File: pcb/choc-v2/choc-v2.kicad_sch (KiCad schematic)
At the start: 139 parts, among them J1 OLED, J2 Conn_01x02_Female, J3 Conn_01x03_Female, SW1 SW_Push, SW2 RotaryEncoder_Switch, SW3 RotaryEncoder_Switch, SW4 SW_SPDT, U1 Elite-C

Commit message: Checkpoint commit.
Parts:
- removed D61, D62, D63, D64, D65: SK6812MINI, footprints:YS-SK6812MINI-E, symbol LED:SK6812MINI
- added D61, D62, D63, D64, D65: SK6812MINI, footprints:YS-SK6812MINI-E, symbol atreyu-pcb2:SK6812MINI_LED
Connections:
- net GND: now also D61.3 (VSS), D62.3 (VSS), D63.3 (VSS), D64.3 (VSS), D65.3 (VSS)
- net LED: now also D61.4 (DIN)
- net VCC: now also D61.1 (VDD), D62.1 (VDD), D63.1 (VDD), D64.1 (VDD), D65.1 (VDD)
- new net: D62.2 (DOUT), D63.4 (DIN)
- new net: D61.2 (DOUT), D62.4 (DIN)
- new net: D64.2 (DOUT), D65.4 (DIN)
- new net: D63.2 (DOUT), D64.4 (DIN)

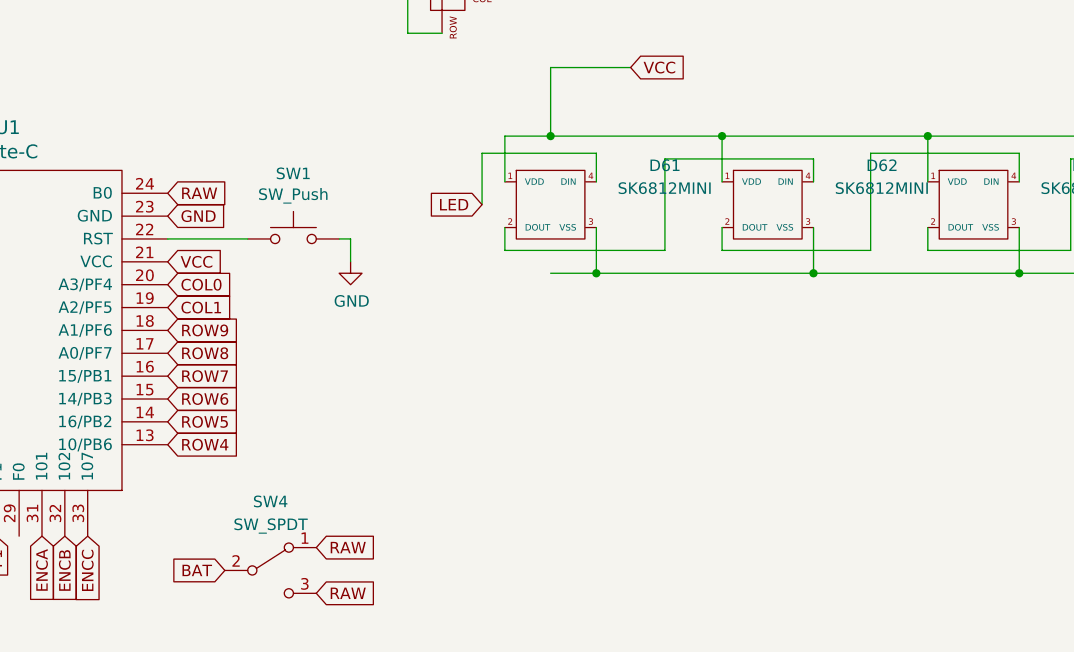
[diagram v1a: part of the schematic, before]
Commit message: Rewired choc v2 pcb.
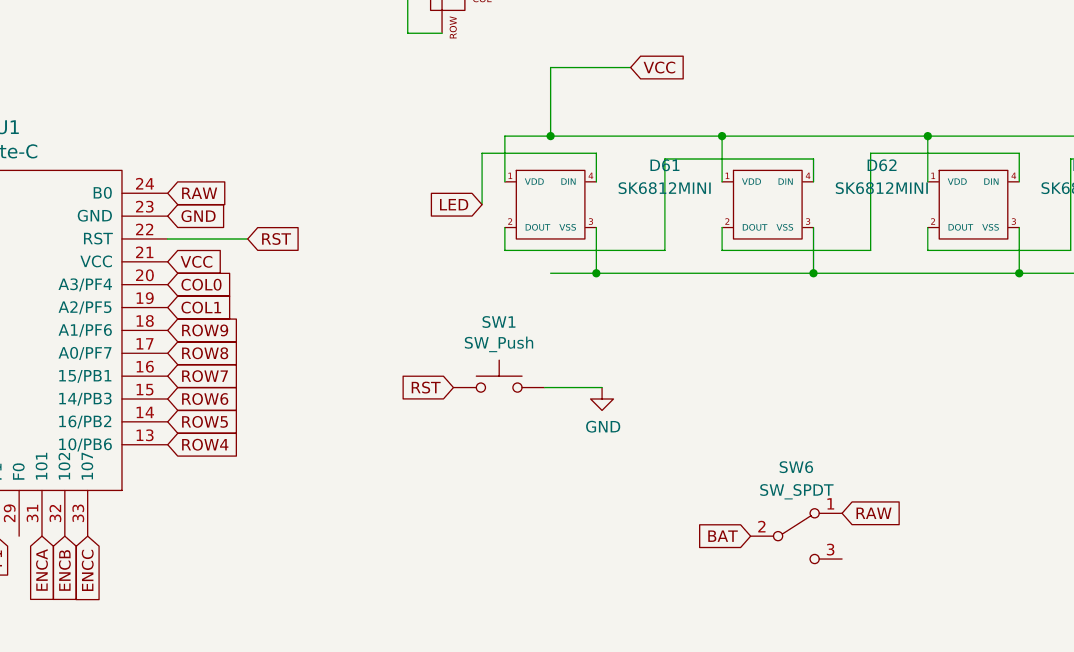
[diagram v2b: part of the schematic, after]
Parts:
- removed SW4: SW_SPDT, footprints:Switch_MSK-12C01-07, symbol Switch:SW_SPDT
- added SW6: SW_SPDT, footprints:Switch_MSK-12C01-07, symbol Switch:SW_SPDT
- SW1: footprint footprints:SW_Tactile_SPST_Angled_MJTP1117_fixed -> footprints:PushSwitch
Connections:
- net BAT: now also SW6.2 (B)
- net RAW: now also SW6.1 (A)
- net RST: now reaches SW1.1, U1.22 (RST)
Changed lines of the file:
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@@
     (stroke (width 0) (type default) (color 0 0 0 0))
   )
-  (wire (pts (xy 82.55 149.86) (xy 83.82 149.86))
-    (stroke (width 0) (type default) (color 0 0 0 0))
-  )
   (wire (pts (xy 91.44 57.15) (xy 93.98 57.15))
     (stroke (width 0) (type default) (color 0 0 0 0))
@@
     (stroke (width 0) (type default) (color 0 0 0 0))
   )
-  (wire (pts (xy 83.82 149.86) (xy 83.82 152.4))
-    (stroke (width 0) (type default) (color 0 0 0 0))
-  )
   (wire (pts (xy 99.06 35.56) (xy 99.06 52.07))
     (stroke (width 0) (type default) (color 0 0 0 0))
@@
     (stroke (width 0) (type default) (color 0 0 0 0))
   )
+  (wire (pts (xy 105.41 166.37) (xy 111.76 166.37))
+    (stroke (width 0) (type default) (color 0 0 0 0))
+  )
   (wire (pts (xy 147.955 138.43) (xy 147.955 143.51))
     (stroke (width 0) (type default) (color 0 0 0 0))
@@
     (stroke (width 0) (type default) (color 0 0 0 0))
   )
+  (global_label "RAW" (shape input) (at 138.43 180.34 0) (fields_autoplaced)
+    (effects (font (size 1.27 1.27)) (justify left))
+    (property "Intersheet References" "${INTERSHEET_REFS}" (id 0) (at 144.6531 180.4194 0)
+      (effects (font (size 1.27 1.27)) (justify left) hide)
+    )
+  )
   (global_label "GND" (shape input) (at 255.27 120.65 180) (fields_autoplaced)
     (effects (font (size 1.27 1.27)) (justify right))
@@
     )
   )
-  (global_label "RAW" (shape input) (at 80.01 189.23 0) (fields_autoplaced)
-    (effects (font (size 1.27 1.27)) (justify left))
-    (property "Intersheet References" "${INTERSHEET_REFS}" (id 0) (at 86.2331 189.3094 0)
-      (effects (font (size 1.27 1.27)) (justify left) hide)
+  (global_label "RST" (shape input) (at 95.25 166.37 180) (fields_autoplaced)
+    (effects (font (size 1.27 1.27)) (justify right))
+    (property "Intersheet References" "${INTERSHEET_REFS}" (id 0) (at 89.3898 166.4494 0)
+      (effects (font (size 1.27 1.27)) (justify right) hide)
     )
   )
@@
     )
   )
-  (global_label "BAT" (shape input) (at 69.85 186.69 180) (fields_autoplaced)
-    (effects (font (size 1.27 1.27)) (justify right))
-    (property "Intersheet References" "${INTERSHEET_REFS}" (id 0) (at 64.1107 186.7694 0)
-      (effects (font (size 1.27 1.27)) (justify right) hide)
-    )
-  )
   (global_label "ROW1" (shape input) (at 31.75 62.23 180) (fields_autoplaced)
     (effects (font (size 1.27 1.27)) (justify right))
@@
     )
   )
-  (global_label "RAW" (shape input) (at 80.01 184.15 0) (fields_autoplaced)
-    (effects (font (size 1.27 1.27)) (justify left))
-    (property "Intersheet References" "${INTERSHEET_REFS}" (id 0) (at 86.2331 184.2294 0)
-      (effects (font (size 1.27 1.27)) (justify left) hide)
-    )
-  )
   (global_label "RAW" (shape input) (at 63.5 144.78 0) (fields_autoplaced)
     (effects (font (size 1.27 1.27)) (justify left))
@@
     )
   )
+  (global_label "BAT" (shape input) (at 128.27 182.88 180) (fields_autoplaced)
+    (effects (font (size 1.27 1.27)) (justify right))
+    (property "Intersheet References" "${INTERSHEET_REFS}" (id 0) (at 122.5307 182.9594 0)
+      (effects (font (size 1.27 1.27)) (justify right) hide)
+    )
+  )
   (global_label "ROW7" (shape input) (at 179.07 77.47 180) (fields_autoplaced)
     (effects (font (size 1.27 1.27)) (justify right))
@@
     )
   )
+  (global_label "RST" (shape input) (at 72.39 149.86 0) (fields_autoplaced)
+    (effects (font (size 1.27 1.27)) (justify left))
+    (property "Intersheet References" "${INTERSHEET_REFS}" (id 0) (at 78.2502 149.7806 0)
+      (effects (font (size 1.27 1.27)) (justify left) hide)
+    )
+  )
   (global_label "ROW8" (shape input) (at 63.5 162.56 0) (fields_autoplaced)
     (effects (font (size 1.27 1.27)) (justify left))
@@
     (pin "2")
   )
+  (symbol (lib_id "power:GND") (at 111.76 166.37 0) (unit 1)
+    (in_bom yes) (on_board yes)
+    (property "Reference" "#PWR0103" (id 0) (at 111.76 172.72 0)
+      (effects (font (size 1.27 1.27)) hide)
+    )
+    (property "Value" "GND" (id 1) (at 111.887 170.7642 0))
+    (property "Footprint" "" (id 2) (at 111.76 166.37 0)
+      (effects (font (size 1.27 1.27)) hide)
+    )
+    (property "Datasheet" "" (id 3) (at 111.76 166.37 0)
+      (effects (font (size 1.27 1.27)) hide)
+    )
+    (pin "1")
+  )
   (symbol (lib_id "MX_Alps_Hybrid:MX-NoLED") (at 200.66 52.07 0) (unit 1)
     (in_bom yes) (on_board yes)
@@
     (pin "2")
   )
+  (symbol (lib_id "Switch:SW_SPDT") (at 133.35 182.88 0) (unit 1)
+    (in_bom yes) (on_board yes) (fields_autoplaced)
+    (property "Reference" "SW6" (id 0) (at 133.35 175.26 0))
+    (property "Value" "SW_SPDT" (id 1) (at 133.35 177.8 0))
+    (property "Footprint" "footprints:Switch_MSK-12C01-07" (id 2) (at 133.35 182.88 0)
+      (effects (font (size 1.27 1.27)) hide)
+    )
+    (property "Datasheet" "~" (id 3) (at 133.35 182.88 0)
+      (effects (font (size 1.27 1.27)) hide)
+    )
+    (pin "1")
+    (pin "2")
+    (pin "3")
+  )
   (symbol (lib_id "Device:D_Small") (at 35.56 92.71 90) (unit 1)
     (in_bom yes) (on_board yes)
@@
     (pin "2")
   )
-  (symbol (lib_id "Switch:SW_SPDT") (at 74.93 186.69 0) (unit 1)
-    (in_bom yes) (on_board yes) (fields_autoplaced)
-    (property "Reference" "SW4" (id 0) (at 74.93 179.07 0))
-    (property "Value" "SW_SPDT" (id 1) (at 74.93 181.61 0))
-    (property "Footprint" "footprints:Switch_MSK-12C01-07" (id 2) (at 74.93 186.69 0)
-      (effects (font (size 1.27 1.27)) hide)
-    )
-    (property "Datasheet" "~" (id 3) (at 74.93 186.69 0)
-      (effects (font (size 1.27 1.27)) hide)
-    )
-    (pin "1")
-    (pin "2")
-    (pin "3")
-  )
   (symbol (lib_id "MX_Alps_Hybrid:MX-NoLED") (at 81.28 69.85 0) (unit 1)
     (in_bom yes) (on_board yes)
@@
     (pin "2")
   )
+  (symbol (lib_id "Switch:SW_Push") (at 100.33 166.37 0) (unit 1)
+    (in_bom yes) (on_board yes)
+    (property "Reference" "SW1" (id 0) (at 100.33 159.131 0))
+    (property "Value" "SW_Push" (id 1) (at 100.33 161.4424 0))
+    (property "Footprint" "footprints:PushSwitch" (id 2) (at 100.33 161.29 0)
+      (effects (font (size 1.27 1.27)) hide)
+    )
+    (property "Datasheet" "~" (id 3) (at 100.33 161.29 0)
+      (effects (font (size 1.27 1.27)) hide)
+    )
+    (pin "1")
+    (pin "2")
+  )
   (symbol (lib_id "Device:D_Small") (at 182.88 58.42 90) (unit 1)
     (in_bom yes) (on_board yes)
@@
     (pin "3")
   )
-  (symbol (lib_id "power:GND") (at 83.82 152.4 0) (unit 1)
-    (in_bom yes) (on_board yes)
-    (property "Reference" "#PWR01" (id 0) (at 83.82 158.75 0)
-      (effects (font (size 1.27 1.27)) hide)
-    )
-    (property "Value" "GND" (id 1) (at 83.947 156.7942 0))
-    (property "Footprint" "" (id 2) (at 83.82 152.4 0)
-      (effects (font (size 1.27 1.27)) hide)
-    )
-    (property "Datasheet" "" (id 3) (at 83.82 152.4 0)
-      (effects (font (size 1.27 1.27)) hide)
-    )
-    (pin "1")
-  )
   (symbol (lib_id "Device:D_Small") (at 63.5 59.69 90) (unit 1)
     (in_bom yes) (on_board yes)
@@
     (pin "2")
   )
-  (symbol (lib_id "Switch:SW_Push") (at 77.47 149.86 0) (unit 1)
-    (in_bom yes) (on_board yes)
-    (property "Reference" "SW1" (id 0) (at 77.47 142.621 0))
-    (property "Value" "SW_Push" (id 1) (at 77.47 144.9324 0))
-    (property "Footprint" "footprints:SW_Tactile_SPST_Angled_MJTP1117_fixed" (id 2) (at 77.47 144.78 0)
-      (effects (font (size 1.27 1.27)) hide)
-    )
-    (property "Datasheet" "~" (id 3) (at 77.47 144.78 0)
-      (effects (font (size 1.27 1.27)) hide)
-    )
-    (pin "1")
-    (pin "2")
-  )
   (symbol (lib_id "Device:D_Small") (at 105.41 76.2 90) (unit 1)
     (in_bom yes) (on_board yes)
@@
   )
   (symbol_instances
-    (path "/ac964def-301e-4952-bb3b-cd9cbd1eebb9"
-      (reference "#PWR01") (unit 1) (value "GND") (footprint "")
-    )
     (path "/2cf3b50e-b2b6-4da6-85da-2865b465c971"
       (reference "#PWR0101") (unit 1) (value "GND") (footprint "")
@@
       (reference "#PWR0102") (unit 1) (value "GND") (footprint "")
     )
+    (path "/4c048a5f-951f-4e43-b2cb-806479581f74"
+      (reference "#PWR0103") (unit 1) (value "GND") (footprint "")
+    )
     (path "/9a4f2410-f69c-4a83-ba00-00b0351bca24"
       (reference "D1") (unit 1) (value "D_Small") (footprint "footprints:D3_hybrid_common_hole_connected_fix")
@@
       (reference "MX62") (unit 1) (value "MX-NoLED") (footprint "footprints:Choc_Hotswap_Solder_18x17")
     )
-    (path "/f228d0b8-6193-4b01-bde8-b5aa48a06a4d"
-      (reference "SW1") (unit 1) (value "SW_Push") (footprint "footprints:SW_Tactile_SPST_Angled_MJTP1117_fixed")
+    (path "/a024f1bb-d59b-4877-95a4-9de14029e719"
+      (reference "SW1") (unit 1) (value "SW_Push") (footprint "footprints:PushSwitch")
     )
     (path "/726b4788-4eb6-41d6-b1fb-ac076eabdb2c"
@@
       (reference "SW3") (unit 1) (value "RotaryEncoder_Switch") (footprint "footprints:RotaryEncoder_EC11")
     )
-    (path "/9ce24d3f-ec81-4be1-9c99-1bd29e5f7113"
-      (reference "SW4") (unit 1) (value "SW_SPDT") (footprint "footprints:Switch_MSK-12C01-07")
+    (path "/9b24b342-1705-440c-96b6-ae4e781dec06"
+      (reference "SW6") (unit 1) (value "SW_SPDT") (footprint "footprints:Switch_MSK-12C01-07")
     )
     (path "/55d3bb9a-fd07-47f6-ac8c-0b322236c705"
